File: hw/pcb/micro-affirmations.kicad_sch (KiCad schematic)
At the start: 0 parts

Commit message: feat: completed initail hardware design
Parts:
- added C1: 15F, micro-affirmations_footprints:CP_Radial_L32.0mm_D12.5mm_P5.00mm_Horizontal, symbol Device:C_Polarized
- added C2: 4.7u, Capacitor_SMD:C_0805_2012Metric, symbol Device:C
- added C3, C4, C5: 100n, Capacitor_SMD:C_0805_2012Metric, symbol Device:C
- added D1: 3V0, Diode_SMD:D_SOD-323, symbol Device:D_Zener
- added D2, D3, D4: TVS, Diode_SMD:D_SOD-923, symbol Device:D_Zener
- added J1: USB-C_2171750001, micro-affirmations_footprints:2171750001_MOL, symbol micro-affirmations_symbols:USB-C_2171750001
- added R1, R2: 5.1k, Resistor_SMD:R_0603_1608Metric, symbol Device:R
- added R3: 100, Resistor_SMD:R_0603_1608Metric, symbol Device:R
- added R4, R5: 10k, Resistor_SMD:R_0603_1608Metric, symbol Device:R
- added SW1: SW_Push, micro-affirmations_footprints:TL1030_A, symbol Switch:SW_Push
- added U1: STM32C031C6Tx, Package_QFP:LQFP-48_7x7mm_P0.5mm, symbol MCU_ST_STM32C0:STM32C031C6Tx
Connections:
- new net: J1.B5 (CC2), R2.1
- new net: J1.A5 (CC1), R1.1
- new net +3V0: C1.1, C2.1, C3.1, C4.1, D1.1 (K), R3.2, U1.11 (PA0), U1.5 (VREF+), U1.6 (VDD)
- new net +5V: J1.A9 (VBUS), J1.B9 (VBUS), R3.1, R4.2
- new net CHARGE_SENSE: R4.1, R5.2, U1.4 (PF3)
- new net DEBUG_SWCLK: D2.1 (K), U1.2 (PC14)
- new net DEBUG_SWDIO: D3.1 (K), U1.1 (PC13)
- new net GND: C1.2, C2.2, C3.2, C4.2, C5.2, D1.2 (A), D2.2 (A), D3.2 (A), D4.2 (A), J1.A12 (GND), J1.B12 (GND), R1.2, R2.2, R5.1, SW1.1, U1.7 (VSS)
- new net MATRIX_A0: U1.38 (PD0)
- new net MATRIX_A1: U1.37 (PA15)
- new net MATRIX_A2: U1.32 (PA10)
- new net MATRIX_A3: U1.31 (PC7)
- new net MATRIX_A4: U1.30 (PC6)
- new net MATRIX_A5: U1.29 (PA9)
- new net MATRIX_A6: U1.28 (PA8)
- new net MATRIX_A7: U1.27 (PB15)
- new net MATRIX_A8: U1.26 (PB14)
- new net MATRIX_A9: U1.25 (PB13)
- new net MATRIX_K0: U1.23 (PB11)
- new net MATRIX_K1: U1.22 (PB10)
- new net MATRIX_K2: U1.21 (PB2)
- new net MATRIX_K3: U1.20 (PB1)
- new net MATRIX_K4: U1.19 (PB0)
- new net MATRIX_K5: U1.18 (PA7)
- new net MATRIX_K6: U1.17 (PA6)
- new net MATRIX_K7: U1.16 (PA5)
- new net MATRIX_K8: U1.15 (PA4)
- new net MATRIX_K9: U1.14 (PA3)
- new net NRST: C5.1, D4.1 (K), SW1.2, U1.10 (PF2)
- new net RANDOM: U1.12 (PA1)
- no-connect marks 0 -> 1
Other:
- added sheet led-matrix (led-matrix.kicad_sch)
- note added: "Power Supply"
- company: (none) -> Isaac Pawley
- title: (none) -> μAffirmations

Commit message: fix: added programming and debug port to schematic
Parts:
- added J2: DEBUG, Connector_PinSocket_2.54mm:PinSocket_1x04_P2.54mm_Vertical, symbol Connector_Generic:Conn_01x04
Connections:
- net +3V0: now also J2.4 (Pin_4)
- net DEBUG_SWCLK: now also J2.2 (Pin_2)
- net DEBUG_SWDIO: now also J2.3 (Pin_3)
- net GND: now also J2.1 (Pin_1)

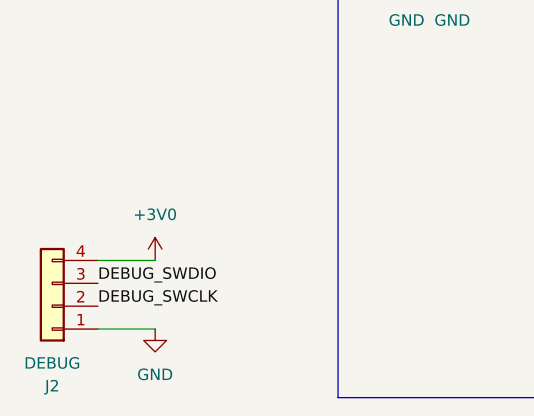
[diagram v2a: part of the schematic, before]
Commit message: fix: updated programming and debug port to include nrst
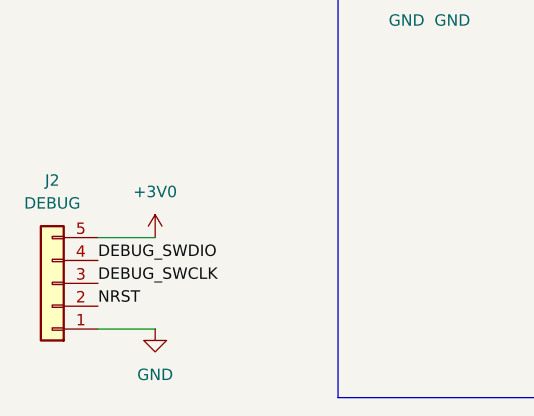
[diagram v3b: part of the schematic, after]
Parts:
- removed J2: DEBUG, Connector_PinSocket_2.54mm:PinSocket_1x04_P2.54mm_Vertical, symbol Connector_Generic:Conn_01x04
- added J2: DEBUG, Connector_PinHeader_2.54mm:PinHeader_1x05_P2.54mm_Vertical, symbol Connector_Generic:Conn_01x05
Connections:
- net +3V0: now also J2.5 (Pin_5)
- net DEBUG_SWCLK: now also J2.3 (Pin_3)
- net DEBUG_SWDIO: now also J2.4 (Pin_4)
- net GND: now also J2.1 (Pin_1)
- net NRST: now also J2.2 (Pin_2)
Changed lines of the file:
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@@
 	(wire
 		(pts
-			(xy 38.1 172.72) (xy 31.75 172.72)
+			(xy 38.1 170.18) (xy 31.75 170.18)
 		)
 		(stroke
@@
 	)
 	(label "DEBUG_SWDIO"
-		(at 31.75 175.26 0)
+		(at 31.75 172.72 0)
 		(effects
 			(font
@@
 	)
 	(label "DEBUG_SWCLK"
-		(at 31.75 177.8 0)
+		(at 31.75 175.26 0)
 		(effects
 			(font
@@
 		)
 	)
+	(label "NRST"
+		(at 31.75 177.8 0)
+		(effects
+			(font
+				(size 1.27 1.27)
+				(thickness 0.1588)
+			)
+			(justify left bottom)
+		)
+	)
 	(label "MATRIX_K0"
 		(at 124.46 163.83 180)
@@
 	(symbol
 		(lib_id "power:+3V0")
-		(at 38.1 172.72 0)
+		(at 38.1 170.18 0)
 		(unit 1)
 		(body_style 1)
@@
 		(fields_autoplaced yes)
 		(property "Reference" "#PWR033"
-			(at 38.1 176.53 0)
+			(at 38.1 173.99 0)
 			(hide yes)
 			(show_name no)
@@
 		)
 		(property "Value" "+3V0"
-			(at 38.1 167.64 0)
+			(at 38.1 165.1 0)
 			(show_name no)
 			(do_not_autoplace no)
@@
 		)
 		(property "Footprint" ""
-			(at 38.1 172.72 0)
+			(at 38.1 170.18 0)
 			(hide yes)
 			(show_name no)
@@
 		)
 		(property "Datasheet" ""
-			(at 38.1 172.72 0)
+			(at 38.1 170.18 0)
 			(hide yes)
 			(show_name no)
@@
 		)
 		(property "Description" "Power symbol creates a global label with name \"+3V0\""
-			(at 38.1 172.72 0)
+			(at 38.1 170.18 0)
 			(hide yes)
 			(show_name no)
@@
 	)
 	(symbol
-		(lib_id "Device:C_Polarized")
-		(at 147.32 40.64 0)
+		(lib_id "Connector_Generic:Conn_01x05")
+		(at 26.67 175.26 180)
 		(unit 1)
 		(body_style 1)
@@
 		(dnp no)
 		(fields_autoplaced yes)
-		(property "Reference" "C1"
-			(at 151.13 38.4809 0)
+		(property "Reference" "J2"
+			(at 26.67 163.83 0)
 			(show_name no)
 			(do_not_autoplace no)
@@
 					(size 1.27 1.27)
 				)
-				(justify left)
 			)
 		)
-		(property "Value" "15F"
-			(at 151.13 41.0209 0)
+		(property "Value" "DEBUG"
+			(at 26.67 166.37 0)
 			(show_name no)
 			(do_not_autoplace no)
@@
 					(size 1.27 1.27)
 				)
-				(justify left)
 			)
 		)
-		(property "Footprint" "micro-affirmations_footprints:CP_Radial_L32.0mm_D12.5mm_P5.00mm_Horizontal"
-			(at 148.2852 44.45 0)
+		(property "Footprint" "Connector_PinHeader_2.54mm:PinHeader_1x05_P2.54mm_Vertical"
+			(at 26.67 175.26 0)
 			(hide yes)
 			(show_name no)
@@
 		)
 		(property "Datasheet" ""
-			(at 147.32 40.64 0)
+			(at 26.67 175.26 0)
 			(hide yes)
 			(show_name no)
@@
 			)
 		)
-		(property "Description" "Polarized capacitor"
-			(at 147.32 40.64 0)
+		(property "Description" "Generic connector, single row, 01x05, script generated (kicad-library-utils/schlib/autogen/connector/)"
+			(at 26.67 175.26 0)
 			(hide yes)
 			(show_name no)
@@
 			)
 		)
+		(pin "5"
+		)
+		(pin "4"
+		)
+		(pin "3"
+		)
 		(pin "2"
 		)
@@
 			(project "micro-affirmations"
 				(path "/5bc9bd8c-4e85-4538-85a6-329775c75541"
-					(reference "C1")
+					(reference "J2")
 					(unit 1)
 				)
@@
 	)
 	(symbol
-		(lib_id "power:+5V")
-		(at 92.71 33.02 0)
+		(lib_id "Device:C_Polarized")
+		(at 147.32 40.64 0)
 		(unit 1)
 		(body_style 1)
@@
 		(dnp no)
 		(fields_autoplaced yes)
-		(property "Reference" "#PWR04"
-			(at 92.71 36.83 0)
-			(hide yes)
+		(property "Reference" "C1"
+			(at 151.13 38.4809 0)
 			(show_name no)
 			(do_not_autoplace no)
@@
 					(size 1.27 1.27)
 				)
+				(justify left)
 			)
 		)
-		(property "Value" "+5V"
-			(at 92.71 27.94 0)
+		(property "Value" "15F"
+			(at 151.13 41.0209 0)
 			(show_name no)
 			(do_not_autoplace no)
@@
 					(size 1.27 1.27)
 				)
+				(justify left)
 			)
 		)
-		(property "Footprint" ""
-			(at 92.71 33.02 0)
+		(property "Footprint" "micro-affirmations_footprints:CP_Radial_L32.0mm_D12.5mm_P5.00mm_Horizontal"
+			(at 148.2852 44.45 0)
 			(hide yes)
 			(show_name no)
@@
 		)
 		(property "Datasheet" ""
-			(at 92.71 33.02 0)
+			(at 147.32 40.64 0)
 			(hide yes)
 			(show_name no)
@@
 			)
 		)
-		(property "Description" "Power symbol creates a global label with name \"+5V\""
-			(at 92.71 33.02 0)
+		(property "Description" "Polarized capacitor"
+			(at 147.32 40.64 0)
 			(hide yes)
 			(show_name no)
@@
 			)
 		)
+		(pin "2"
+		)
 		(pin "1"
 		)
@@
 			(project "micro-affirmations"
 				(path "/5bc9bd8c-4e85-4538-85a6-329775c75541"
-					(reference "#PWR04")
+					(reference "C1")
 					(unit 1)
 				)
@@
 	(symbol
 		(lib_id "power:+5V")
-		(at 46.99 33.02 0)
+		(at 92.71 33.02 0)
 		(unit 1)
 		(body_style 1)
@@
 		(dnp no)
 		(fields_autoplaced yes)
-		(property "Reference" "#PWR06"
-			(at 46.99 36.83 0)
+		(property "Reference" "#PWR04"
+			(at 92.71 36.83 0)
 			(hide yes)
 			(show_name no)
@@
 		)
 		(property "Value" "+5V"
-			(at 46.99 27.94 0)
+			(at 92.71 27.94 0)
 			(show_name no)
 			(do_not_autoplace no)
@@
 		)
 		(property "Footprint" ""
-			(at 46.99 33.02 0)
+			(at 92.71 33.02 0)
 			(hide yes)
 			(show_name no)
@@
 		)
 		(property "Datasheet" ""
-			(at 46.99 33.02 0)
+			(at 92.71 33.02 0)
 			(hide yes)
 			(show_name no)
@@
 		)
 		(property "Description" "Power symbol creates a global label with name \"+5V\""
-			(at 46.99 33.02 0)
+			(at 92.71 33.02 0)
 			(hide yes)
 			(show_name no)
@@
 			(project "micro-affirmations"
 				(path "/5bc9bd8c-4e85-4538-85a6-329775c75541"
-					(reference "#PWR06")
+					(reference "#PWR04")
 					(unit 1)
 				)
@@
 	)
 	(symbol
-		(lib_id "power:GND")
-		(at 38.1 180.34 0)
+		(lib_id "power:+5V")
+		(at 46.99 33.02 0)
 		(unit 1)
 		(body_style 1)
@@
 		(dnp no)
 		(fields_autoplaced yes)
-		(property "Reference" "#PWR032"
-			(at 38.1 186.69 0)
+		(property "Reference" "#PWR06"
+			(at 46.99 36.83 0)
 			(hide yes)
 			(show_name no)
@@
 			)
 		)
-		(property "Value" "GND"
-			(at 38.1 185.42 0)
+		(property "Value" "+5V"
+			(at 46.99 27.94 0)
 			(show_name no)
 			(do_not_autoplace no)
@@
 		)
 		(property "Footprint" ""
-			(at 38.1 180.34 0)
+			(at 46.99 33.02 0)
 			(hide yes)
 			(show_name no)
@@
 		)
 		(property "Datasheet" ""
-			(at 38.1 180.34 0)
+			(at 46.99 33.02 0)
 			(hide yes)
 			(show_name no)
@@
 			)
 		)
-		(property "Description" "Power symbol creates a global label with name \"GND\" , ground"
-			(at 38.1 180.34 0)
+		(property "Description" "Power symbol creates a global label with name \"+5V\""
+			(at 46.99 33.02 0)
 			(hide yes)
 			(show_name no)
@@
 			(project "micro-affirmations"
 				(path "/5bc9bd8c-4e85-4538-85a6-329775c75541"
-					(reference "#PWR032")
+					(reference "#PWR06")
 					(unit 1)
 				)
@@
 	)
 	(symbol
-		(lib_id "Connector_Generic:Conn_01x04")
-		(at 26.67 177.8 180)
+		(lib_id "power:GND")
+		(at 38.1 180.34 0)
 		(unit 1)
 		(body_style 1)
@@
 		(in_pos_files yes)
 		(dnp no)
-		(property "Reference" "J2"
-			(at 26.67 186.69 0)
+		(fields_autoplaced yes)
+		(property "Reference" "#PWR032"
+			(at 38.1 186.69 0)
+			(hide yes)
 			(show_name no)
 			(do_not_autoplace no)
@@
 			)
 		)
-		(property "Value" "DEBUG"
-			(at 26.67 184.15 0)
+		(property "Value" "GND"
+			(at 38.1 185.42 0)
 			(show_name no)
 			(do_not_autoplace no)
@@
 			)
 		)
-		(property "Footprint" "Connector_PinSocket_2.54mm:PinSocket_1x04_P2.54mm_Vertical"
-			(at 26.67 177.8 0)
+		(property "Footprint" ""
+			(at 38.1 180.34 0)
 			(hide yes)
 			(show_name no)
@@
 		)
 		(property "Datasheet" ""
-			(at 26.67 177.8 0)
+			(at 38.1 180.34 0)
 			(hide yes)
 			(show_name no)
@@
 			)
 		)
-		(property "Description" "Generic connector, single row, 01x04, script generated (kicad-library-utils/schlib/autogen/connector/)"
-			(at 26.67 177.8 0)
+		(property "Description" "Power symbol creates a global label with name \"GND\" , ground"
+			(at 38.1 180.34 0)
 			(hide yes)
 			(show_name no)
@@
 		(pin "1"
 		)
-		(pin "4"
-		)
-		(pin "3"
-		)
-		(pin "2"
-		)
 		(instances
 			(project "micro-affirmations"
 				(path "/5bc9bd8c-4e85-4538-85a6-329775c75541"
-					(reference "J2")
+					(reference "#PWR032")
 					(unit 1)
 				)

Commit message: feat: completed pcb layout for revision a
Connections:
- net MATRIX_A0: now also U1.29 (PA9); no longer U1.38 (PD0)
- net MATRIX_A1: now also U1.28 (PA8); no longer U1.37 (PA15)
- net MATRIX_A2: now also U1.27 (PB15); no longer U1.32 (PA10)
- net MATRIX_A3: now also U1.26 (PB14); no longer U1.31 (PC7)
- net MATRIX_A4: now also U1.25 (PB13); no longer U1.30 (PC6)
- net MATRIX_A5: now also U1.30 (PC6); no longer U1.29 (PA9)
- net MATRIX_A6: now also U1.31 (PC7); no longer U1.28 (PA8)
- net MATRIX_A7: now also U1.32 (PA10); no longer U1.27 (PB15)
- net MATRIX_A8: now also U1.37 (PA15); no longer U1.26 (PB14)
- net MATRIX_A9: now also U1.38 (PD0); no longer U1.25 (PB13)
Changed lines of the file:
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@@
+		)
+	)
+	(label "MATRIX_A0"
+		(at 124.46 115.57 180)
+		(effects
+			(font
+				(size 1.27 1.27)
+			)
+			(justify right bottom)
 		)
 	)
@@
 	)
 	(label "MATRIX_A4"
-		(at 64.77 123.19 0)
-		(effects
-			(font
-				(size 1.27 1.27)
-			)
-			(justify left bottom)
-		)
-	)
-	(label "MATRIX_A4"
 		(at 190.5 48.26 0)
 		(effects
@@
 		)
 	)
-	(label "MATRIX_A9"
-		(at 124.46 168.91 180)
-		(effects
-			(font
-				(size 1.27 1.27)
-			)
-			(justify right bottom)
-		)
-	)
 	(label "MATRIX_K6"
 		(at 252.73 53.34 180)
@@
 		)
 	)
+	(label "MATRIX_A8"
+		(at 124.46 130.81 180)
+		(effects
+			(font
+				(size 1.27 1.27)
+			)
+			(justify right bottom)
+		)
+	)
 	(label "MATRIX_K2"
 		(at 124.46 140.97 180)
@@
 		)
 	)
+	(label "MATRIX_A4"
+		(at 124.46 168.91 180)
+		(effects
+			(font
+				(size 1.27 1.27)
+			)
+			(justify right bottom)
+		)
+	)
 	(label "MATRIX_A9"
 		(at 190.5 60.96 0)
@@
 		)
 	)
-	(label "MATRIX_A5"
-		(at 124.46 115.57 180)
-		(effects
-			(font
-				(size 1.27 1.27)
-			)
-			(justify right bottom)
-		)
-	)
 	(label "MATRIX_A[0..9]"
 		(at 144.78 97.79 0)
@@
 	)
 	(label "MATRIX_A8"
-		(at 124.46 171.45 180)
-		(effects
-			(font
-				(size 1.27 1.27)
-			)
-			(justify right bottom)
-		)
-	)
-	(label "MATRIX_A8"
 		(at 190.5 58.42 0)
 		(effects
@@
 		)
 	)
-	(label "MATRIX_A0"
-		(at 64.77 110.49 0)
-		(effects
-			(font
-				(size 1.27 1.27)
-			)
-			(justify left bottom)
-		)
-	)
 	(label "MATRIX_K4"
 		(at 124.46 135.89 180)
@@
 		)
 	)
-	(label "MATRIX_A7"
-		(at 124.46 173.99 180)
-		(effects
-			(font
-				(size 1.27 1.27)
-			)
-			(justify right bottom)
-		)
-	)
-	(label "MATRIX_A3"
-		(at 64.77 125.73 0)
-		(effects
-			(font
-				(size 1.27 1.27)
-			)
-			(justify left bottom)
-		)
-	)
 	(label "DEBUG_SWCLK"
 		(at 31.75 175.26 0)
@@
 	)
 	(label "MATRIX_A2"
+		(at 124.46 173.99 180)
+		(effects
+			(font
+				(size 1.27 1.27)
+			)
+			(justify right bottom)
+		)
+	)
+	(label "MATRIX_A7"
 		(at 124.46 118.11 180)
 		(effects
@@
 		)
 	)
-	(label "MATRIX_A1"
-		(at 124.46 130.81 180)
-		(effects
-			(font
-				(size 1.27 1.27)
-			)
-			(justify right bottom)
-		)
-	)
-	(label "MATRIX_A6"
-		(at 124.46 113.03 180)
-		(effects
-			(font
-				(size 1.27 1.27)
-			)
-			(justify right bottom)
+	(label "MATRIX_A5"
+		(at 64.77 123.19 0)
+		(effects
+			(font
+				(size 1.27 1.27)
+			)
+			(justify left bottom)
 		)
 	)
@@
 		)
 	)
+	(label "MATRIX_A1"
+		(at 124.46 113.03 180)
+		(effects
+			(font
+				(size 1.27 1.27)
+			)
+			(justify right bottom)
+		)
+	)
 	(label "MATRIX_A3"
 		(at 190.5 45.72 0)
@@
 		)
 	)
+	(label "MATRIX_A3"
+		(at 124.46 171.45 180)
+		(effects
+			(font
+				(size 1.27 1.27)
+			)
+			(justify right bottom)
+		)
+	)
 	(label "MATRIX_K0"
 		(at 124.46 163.83 180)
@@
 		)
 	)
+	(label "MATRIX_A9"
+		(at 64.77 110.49 0)
+		(effects
+			(font
+				(size 1.27 1.27)
+			)
+			(justify left bottom)
+		)
+	)
 	(label "MATRIX_K8"
 		(at 124.46 102.87 180)
@@
 		)
 	)
+	(label "MATRIX_A6"
+		(at 64.77 125.73 0)
+		(effects
+			(font
+				(size 1.27 1.27)
+			)
+			(justify left bottom)
+		)
+	)
